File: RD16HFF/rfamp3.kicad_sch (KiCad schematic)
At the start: 56 parts, among them J1 Conn_Coaxial, J2 LPF-Out, J3 Conn_Coaxial, J4 LPF, J5 12V Power, J6 12V Switch, K1 G5V-2, K2 G5V-2, Q1 2N3906, Q2 RD06HHF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

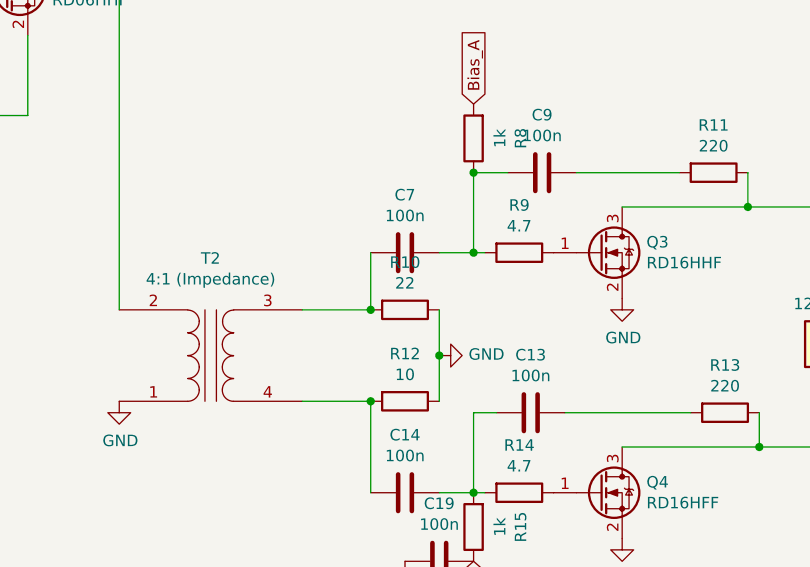
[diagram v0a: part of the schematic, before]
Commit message: add RD16HFF version
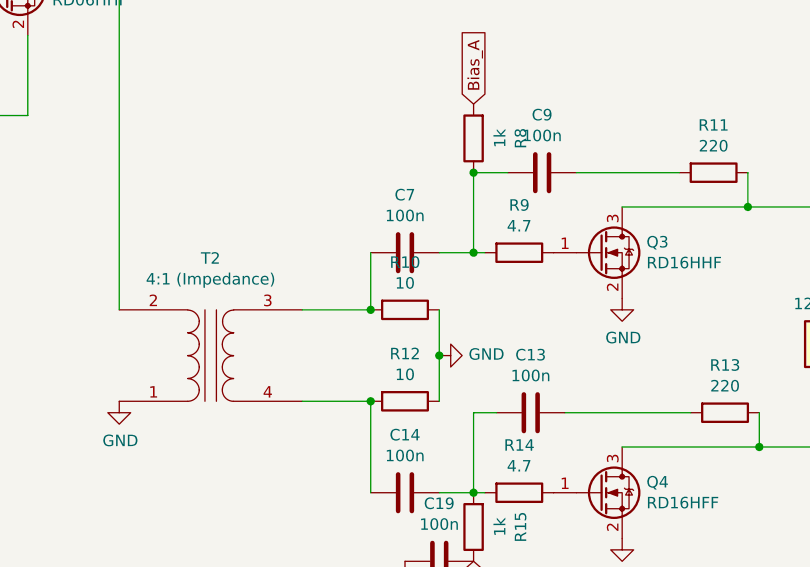
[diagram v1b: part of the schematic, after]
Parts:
- R10: value 22 -> 10
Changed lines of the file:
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@@
     (in_bom yes) (on_board yes)
     (property "Reference" "R10" (id 0) (at 143.51 106.5022 90))
-    (property "Value" "22" (id 1) (at 143.51 108.8136 90))
+    (property "Value" "10" (id 1) (at 143.51 108.8136 90))
     (property "Footprint" "Resistor_SMD:R_2512_6332Metric" (id 2) (at 143.51 109.982 90)
       (effects (font (size 1.27 1.27)) hide)
@@
     )
     (path "/00000000-0000-0000-0000-00005d85cc4a"
-      (reference "R10") (unit 1) (value "22") (footprint "Resistor_SMD:R_2512_6332Metric")
+      (reference "R10") (unit 1) (value "10") (footprint "Resistor_SMD:R_2512_6332Metric")
     )
     (path "/00000000-0000-0000-0000-00005d9ed916"
